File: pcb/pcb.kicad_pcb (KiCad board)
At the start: 4 copper layers, 107 parts, among them J1 Conn_02x10_Odd_Even, J2 Conn_02x03_Counter_Clockwise, Q1 BSS138, Q10 BSS138, Q11 BSS138, Q12 BSS138, Q2 BSS138, Q3 BSS138, Q4 BSS138, Q5 BSS138, Q6 BSS138, Q7 BSS138, Q8 BSS138, Q9 BSS138, SW1 SW_PUSHBUTTON, SW2 SW_PUSHBUTTON, SW3 SW_PUSHBUTTON, SW4 SW_PUSHBUTTON, U1 EFM32GG980, U2 ARDUINO_PYNQ_SHIELD, U3 IMU, U4 lidar, U5 ULTRASONIC-GPIO, U6 ULTRASONIC-GPIO, U7 ULTRASONIC-GPIO, Y1 Crystal_GND23

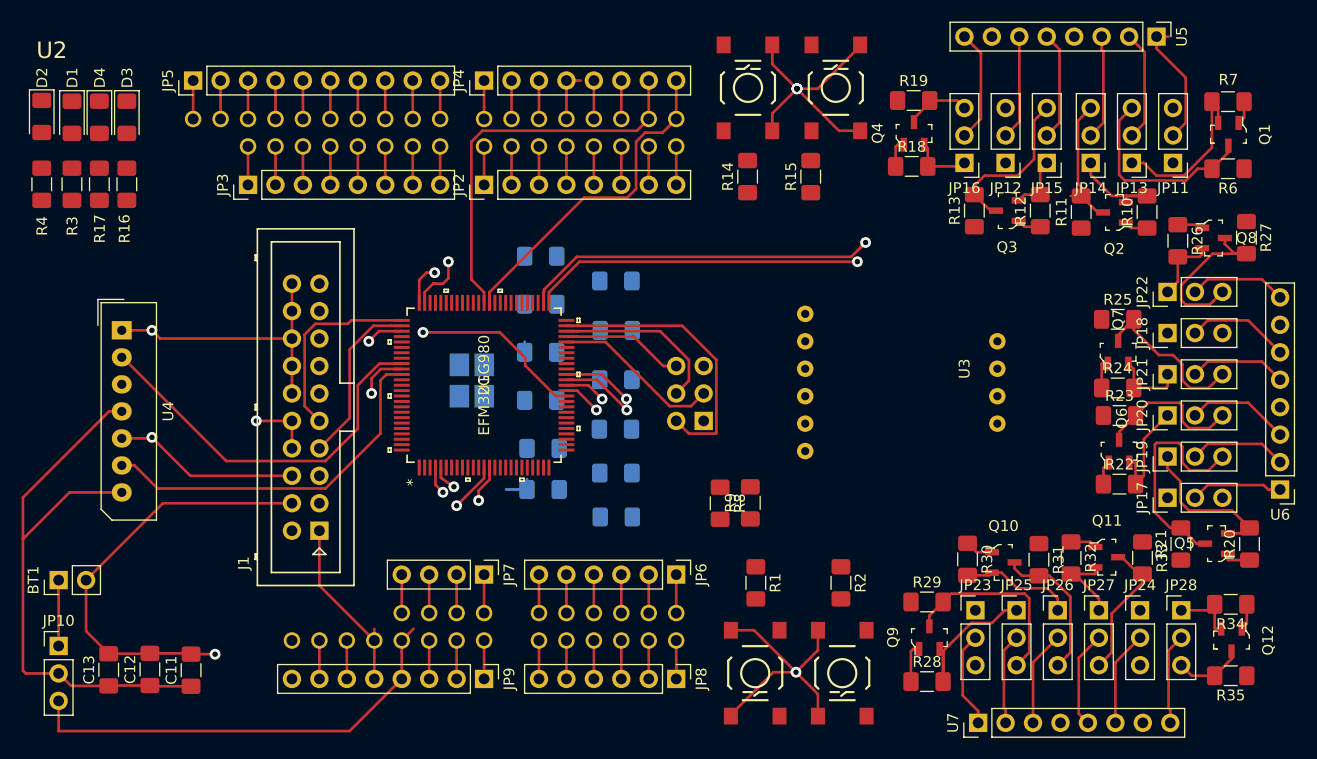
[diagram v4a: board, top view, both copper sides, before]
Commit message: Connect some more wires
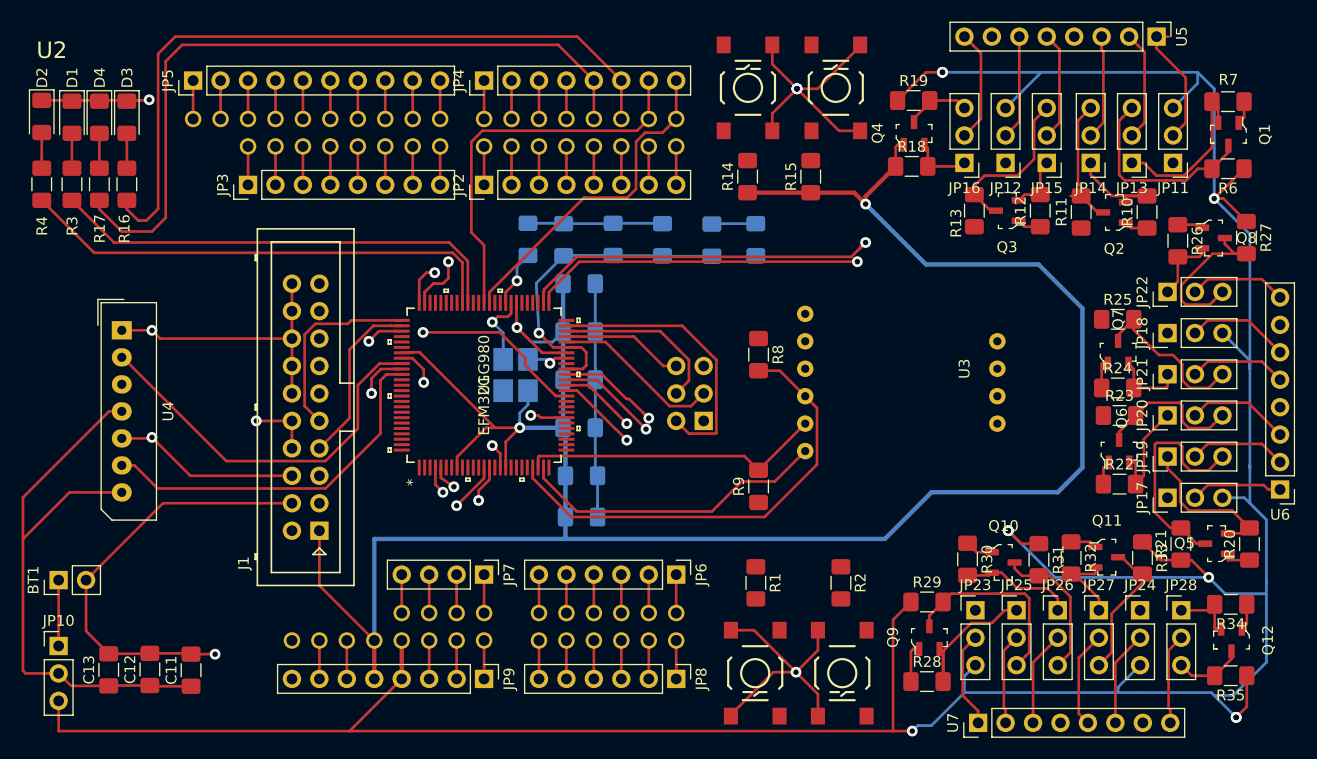
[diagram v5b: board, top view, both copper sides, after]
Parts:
- moved C10 27.0 mm to (105.7, 64.5), turned to 270 degrees
- moved L1 25.2 mm to (126.7, 64.5), turned to 90 degrees
- moved R5 19.6 mm to (122.7, 64.6), turned to 270 degrees
- moved R8 14.2 mm to (127.0, 75.1)
- moved C7 13.7 mm to (118.1, 64.5), turned to 90 degrees
- moved C5 8.42 mm to (113.5, 64.5), turned to 90 degrees
- moved C2 6.15 mm to (109.0, 64.5), turned to 90 degrees
- moved C3 4.37 mm to (110.4, 73.0)
- moved C6 4.37 mm to (110.4, 81.9)
- moved C8 4.37 mm to (110.6, 86.4)
- moved C9 4.37 mm to (110.6, 90.2)
- moved C1 4.37 mm to (110.4, 68.6)
- moved C4 4.37 mm to (110.4, 77.5)
- moved Y1 4.08 mm to (104.5, 77.0)
- moved R9 1.70 mm to (127.0, 87.3)
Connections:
- R1 pad 2: /EFM_DEBUG/SW_1 -> /PC1
- R2 pad 2: /EFM_DEBUG/SW_2 -> /PC0
- SW1 pad 1: /EFM_DEBUG/SW_1 -> /PC1
- SW2 pad 1: /EFM_DEBUG/SW_2 -> /PC0
- U1 pad 1: /EFM_DEBUG/LED_1 -> Net-(U1-Pad1)
- U1 pad 18: Net-(U1-Pad18) -> /PC0
- U1 pad 19: Net-(U1-Pad19) -> /PC1
- U1 pad 2: /EFM_DEBUG/LED_2 -> Net-(U1-Pad2)
- U1 pad 66: Net-(U1-Pad66) -> /EFM_DEBUG/LED_1
- U1 pad 67: Net-(U1-Pad67) -> /EFM_DEBUG/LED_2
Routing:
- net VCC: track 41.6 -> 301.4 mm, vias 0 -> 9
- net +3V3: track 51.4 -> 247.8 mm, vias 0 -> 3
- net GND: track 167.4 -> 232.9 mm, vias 8 -> 13
- net /PYNQ-DEBUG/LED_2: track 3.56 -> 68.0 mm
- net /PYNQ-DEBUG/LED_1: track 3.56 -> 67.7 mm
- net /EFM_DEBUG/LED_2: track 0.00 -> 45.0 mm
- net /IMU/SDA: track 0.00 -> 42.9 mm
- net /EFM_DEBUG/LED_1: track 0.00 -> 42.8 mm
- net /AVDD_DEC: track 0.15 -> 33.0 mm, vias 0 -> 1
- net /IMU/RST: track 0.00 -> 28.8 mm
- net /IMU/SCL: track 0.00 -> 28.1 mm
- net /PB9: track 68.8 -> 74.8 mm
- net /DEC: track 0.00 -> 5.25 mm, vias 0 -> 1
- net Net-(L1-Pad2): track 0.00 -> 4.08 mm
- net /CLOCK/HFXTAL_N: track 0.00 -> 3.90 mm, vias 0 -> 1
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
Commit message: Think it is somewhat finished
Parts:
- removed JP11, JP12, JP13, JP14, JP15, JP16, JP17, JP18, JP19, JP20, JP21, JP22, JP23, JP24, JP25, JP26, JP27, JP28: Jumper_NC_Dual, Connector_PinHeader_2.54mm:PinHeader_1x03_P2.54mm_Vertical
- added JP1: M08, Connector_PinHeader_2.54mm:PinHeader_1x08_P2.54mm_Vertical, F.Cu at (101.6, 59.2)
- added SW10: SW_2xSPDT, localization-footprints:CAS-D20TB, F.Cu at (160.5, 101.6)
- added SW11: SW_2xSPDT, localization-footprints:CAS-D20TB, F.Cu at (169.4, 101.6)
- added SW12: SW_PUSHBUTTON, myfootprint:SW_PUSHBUTTON_SMD, F.Cu at (129.8, 52.0)
- added SW13: SW_PUSHBUTTON, myfootprint:SW_PUSHBUTTON_SMD, F.Cu at (138.4, 52.0)
- added SW5: SW_2xSPDT, localization-footprints:CAS-D20TB, F.Cu at (167.4, 88.4)
- added SW6: SW_2xSPDT, localization-footprints:CAS-D20TB, F.Cu at (150.9, 52.8)
- added SW7: SW_2xSPDT, localization-footprints:CAS-D20TB, F.Cu at (167.4, 79.2)
- added SW8: SW_2xSPDT, localization-footprints:CAS-D20TB, F.Cu at (167.4, 70.1)
- added SW9: SW_2xSPDT, localization-footprints:CAS-D20TB, F.Cu at (151.6, 101.6)
- C11, C12, C13, Q1, Q10, Q11, Q12, Q2, Q3, Q4, Q5, Q6, Q7, Q8, Q9, R10, R11, R12, R13, R18, R19, R20, R21, R22, R23, R24, R25, R26, R27, R28, R29, R30, R31: moved to B.Cu
- JP4: value M08 -> M10; footprint Connector_PinHeader_2.54mm:PinHeader_1x08_P2.54mm_Vertical -> Connector_PinHeader_2.54mm:PinHeader_1x10_P2.54mm_Vertical
- JP5: value M10 -> M06; footprint Connector_PinHeader_2.54mm:PinHeader_1x10_P2.54mm_Vertical -> Connector_PinHeader_2.54mm:PinHeader_1x06_P2.54mm_Vertical
- JP6: value M06 -> M04; footprint Connector_PinHeader_2.54mm:PinHeader_1x06_P2.54mm_Vertical -> Connector_PinHeader_2.54mm:PinHeader_1x04_P2.54mm_Vertical
- JP7: value M04 -> M06; footprint Connector_PinHeader_2.54mm:PinHeader_1x04_P2.54mm_Vertical -> Connector_PinHeader_2.54mm:PinHeader_1x06_P2.54mm_Vertical
- JP8: value M06 -> M08; footprint Connector_PinHeader_2.54mm:PinHeader_1x06_P2.54mm_Vertical -> Connector_PinHeader_2.54mm:PinHeader_1x08_P2.54mm_Vertical
- JP9: value M08 -> Jumper_NC_Dual; footprint Connector_PinHeader_2.54mm:PinHeader_1x08_P2.54mm_Vertical -> Connector_PinHeader_2.54mm:PinHeader_1x03_P2.54mm_Vertical
- R14, R15, R16, R17: value R -> 10k; moved to B.Cu
- R32, R33, R34, R35: value 10k -> R
- R6: value 10k -> 2.2k; moved to B.Cu
- R7: value 10k -> 4.7k; moved to B.Cu
- R8: value 2.2k -> 10k; moved to B.Cu
- R9: value 4.7k -> 10k; moved to B.Cu
- SW3, SW4: value SW_PUSHBUTTON -> SW_2xSPDT; footprint myfootprint:SW_PUSHBUTTON_SMD -> localization-footprints:CAS-D20TB
- moved R35 115.7 mm to (65.5, 56.6), turned to 90 degrees
- moved R34 110.7 mm to (68.1, 56.6), turned to 90 degrees
- moved R17 93.3 mm to (159.0, 51.8), turned to 270 degrees
- moved R16 87.7 mm to (156.2, 56.4), turned to 180 degrees
- moved SW2 79.3 mm to (63.8, 69.3), turned to 0 degrees
- moved R2 71.7 mm to (70.6, 64.0)
- moved SW1 68.5 mm to (63.8, 77.5), turned to 0 degrees
- moved JP5 64.1 mm to (119.4, 95.8), turned to 270 degrees
- moved R1 62.6 mm to (73.2, 64.0)
- moved R9 57.7 mm to (172.5, 51.8), turned to 270 degrees
- moved R8 46.4 mm to (169.4, 56.4), turned to 180 degrees
- moved R15 45.5 mm to (168.9, 85.1), turned to 180 degrees
- moved R14 45.0 mm to (164.3, 82.3)
- moved R32 43.8 mm to (127.8, 60.5), turned to 90 degrees
- moved R21 43.1 mm to (152.4, 51.8), turned to 270 degrees
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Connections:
- JP10 pad 1: Net-(BT1-Pad1) -> Net-(C11-Pad1)
- JP10 pad 2: Net-(C11-Pad1) -> Net-(JP10-Pad2)
- JP3 pad 3: Net-(JP3-Pad3) -> /PYNQ-DEBUG/LED_2
- JP3 pad 4: Net-(JP3-Pad4) -> /PYNQ-DEBUG/LED_1
- JP3 pad 5: Net-(JP3-Pad5) -> /PYNQ-DEBUG/SW_2
- JP3 pad 6: Net-(JP3-Pad6) -> /PYNQ-DEBUG/SW_1
- JP3 pad 7: Net-(JP3-Pad7) -> /PYNQ_TX
- JP3 pad 8: Net-(JP3-Pad8) -> /PYNQ_RX
- JP4 pad 1: Net-(JP4-Pad1) -> /PYNQ_SCL
- JP4 pad 2: Net-(JP4-Pad2) -> /PYNQ_SDA
- JP4 pad 3: /PYNQ-DEBUG/SW_2 -> Net-(JP4-Pad3)
- JP4 pad 4: /PYNQ-DEBUG/SW_1 -> Net-(JP4-Pad4)
- JP4 pad 5: /PYNQ-DEBUG/LED_2 -> Net-(JP4-Pad5)
- JP4 pad 6: /PYNQ-DEBUG/LED_1 -> Net-(JP4-Pad6)
- JP4 pad 7: /PYNQ_TX -> Net-(JP4-Pad7)
- JP4 pad 8: /PYNQ_RX -> Net-(JP4-Pad8)
- JP5 pad 1: /PYNQ_SCL -> Net-(JP5-Pad1)
- JP5 pad 2: /PYNQ_SDA -> Net-(JP5-Pad2)
- JP8 pad 2: Net-(JP8-Pad2) -> GND
- JP8 pad 3: Net-(JP8-Pad3) -> GND
- JP8 pad 4: Net-(JP8-Pad4) -> VCC
- JP8 pad 5: Net-(JP8-Pad5) -> +3V3
- JP9 pad 1: Net-(JP9-Pad1) -> Net-(BT1-Pad1)
- JP9 pad 2: GND -> Net-(C11-Pad1)
- JP9 pad 3: GND -> VCC
- Q1 pad 2: /PD5 -> /PD6_A1
- Q1 pad 3: Net-(JP13-Pad3) -> Net-(Q1-Pad3)
- Q10 pad 2: /PB5 -> /PC1_B2
- Q10 pad 3: Net-(JP26-Pad3) -> Net-(Q10-Pad3)
- Q11 pad 2: /PA4 -> /PC3_BRX
- Q11 pad 3: Net-(JP27-Pad3) -> Net-(Q11-Pad3)
- Q12 pad 2: /PA3 -> /PC2_BTX
- Q12 pad 3: Net-(JP28-Pad3) -> Net-(Q12-Pad3)
- Q2 pad 2: /PD6 -> /PA7_C1
- Q3 pad 2: /PF11 -> /PD7_A2
- Q3 pad 3: Net-(JP15-Pad3) -> Net-(Q3-Pad3)
- Q4 pad 2: /PF10 -> /PA8_C2
- Q4 pad 3: Net-(JP16-Pad3) -> Net-(Q4-Pad3)
- Q5 pad 2: /PB11 -> /PF11_ARX
- Q5 pad 3: Net-(JP19-Pad3) -> Net-(Q5-Pad3)
- Q6 pad 2: /PB12 -> /PB8_CRX
- Q6 pad 3: Net-(JP20-Pad3) -> Net-(Q6-Pad3)
- Q7 pad 2: /PB10 -> /PF10_ATX
- Q7 pad 3: Net-(JP21-Pad3) -> Net-(Q7-Pad3)
- Q8 pad 2: /PB9 -> /PB7_CTX
- Q8 pad 3: Net-(JP22-Pad3) -> Net-(Q8-Pad3)
- Q9 pad 2: /PB4 -> /PC0_B1
- Q9 pad 3: Net-(JP25-Pad3) -> Net-(Q9-Pad3)
- R1 pad 2: /PC1 -> /EFM_DEBUG/SW_1
- R10 pad 2: /PD6 -> /PA7_C1
- R12 pad 2: /PF11 -> /PD7_A2
- R13 pad 2: Net-(JP15-Pad3) -> Net-(Q3-Pad3)
- R14 pad 2: /PYNQ-DEBUG/SW_1 -> /PA8_C2
- R15 pad 1: +3V3 -> VCC
- R15 pad 2: /PYNQ-DEBUG/SW_2 -> Net-(Q4-Pad3)
- R16 pad 1: /PYNQ-DEBUG/LED_1 -> +3V3
- R16 pad 2: Net-(D3-Pad2) -> /PF11_ARX
- R17 pad 1: /PYNQ-DEBUG/LED_2 -> VCC
- R17 pad 2: Net-(D4-Pad2) -> Net-(Q5-Pad3)
- R18 pad 2: /PF10 -> /PB8_CRX
- R19 pad 2: Net-(JP16-Pad3) -> Net-(Q6-Pad3)
- R2 pad 2: /PC0 -> /EFM_DEBUG/SW_2
- R20 pad 2: /PB11 -> /PF10_ATX
- R21 pad 2: Net-(JP19-Pad3) -> Net-(Q7-Pad3)
- R22 pad 2: /PB12 -> /PB7_CTX
- R23 pad 2: Net-(JP20-Pad3) -> Net-(Q8-Pad3)
- R24 pad 2: /PB10 -> /PC0_B1
- R25 pad 2: Net-(JP21-Pad3) -> Net-(Q9-Pad3)
- R26 pad 2: /PB9 -> /PC1_B2
- R27 pad 2: Net-(JP22-Pad3) -> Net-(Q10-Pad3)
- R28 pad 2: /PB4 -> /PC3_BRX
- R29 pad 2: Net-(JP25-Pad3) -> Net-(Q11-Pad3)
- R30 pad 2: /PB5 -> /PC2_BTX
- R31 pad 2: Net-(JP26-Pad3) -> Net-(Q12-Pad3)
- R32 pad 2: /PA4 -> /PYNQ-DEBUG/SW_1
- R33 pad 1: VCC -> +3V3
- R33 pad 2: Net-(JP27-Pad3) -> /PYNQ-DEBUG/SW_2
- R34 pad 1: +3V3 -> /PYNQ-DEBUG/LED_1
- R34 pad 2: /PA3 -> Net-(D3-Pad2)
- R35 pad 1: VCC -> /PYNQ-DEBUG/LED_2
- R35 pad 2: Net-(JP28-Pad3) -> Net-(D4-Pad2)
- R6 pad 1: VCC -> +3V3
- R6 pad 2: Net-(JP13-Pad3) -> /PB11_IMU_SDA
- R7 pad 2: /PD5 -> /PB12_IMU_SCL
- R8 pad 2: /IMU/SDA -> /PD6_A1
- R9 pad 1: +3V3 -> VCC
- R9 pad 2: /IMU/SCL -> Net-(Q1-Pad3)
- SW1 pad 1: /PC1 -> /EFM_DEBUG/SW_1
- SW2 pad 1: /PC0 -> /EFM_DEBUG/SW_2
- SW3 pad 1: /PYNQ-DEBUG/SW_1 -> VCC
- SW3 pad 2: GND -> Net-(SW3-Pad2)
- SW4 pad 1: /PYNQ-DEBUG/SW_2 -> Net-(Q3-Pad3)
- SW4 pad 2: GND -> Net-(SW4-Pad2)
- U1 pad 13: /PB4 -> Net-(U1-Pad13)
- U1 pad 14: /PB5 -> Net-(U1-Pad14)
- U1 pad 18: /PC0 -> /PC0_B1
- U1 pad 19: /PC1 -> /PC1_B2
- U1 pad 20: Net-(U1-Pad20) -> /PC2_BTX
- U1 pad 21: Net-(U1-Pad21) -> /PC3_BRX
- U1 pad 22: /IMU/SDA -> Net-(U1-Pad22)
- U1 pad 23: /IMU/SCL -> Net-(U1-Pad23)
- U1 pad 24: /IMU/RST -> /PB7_CTX
- U1 pad 25: Net-(U1-Pad25) -> /PB8_CRX
- U1 pad 26: Net-(U1-Pad26) -> /PA7_C1
- U1 pad 27: Net-(U1-Pad27) -> /PA8_C2
- U1 pad 28: Net-(U1-Pad28) -> /PA9_IMU_INT
- U1 pad 37: /PB9 -> Net-(U1-Pad37)
- U1 pad 38: /PB10 -> /PB10_IMU_RST
- U1 pad 39: /PB11 -> /PB11_IMU_SDA
- U1 pad 4: /PA3 -> Net-(U1-Pad4)
- U1 pad 40: /PB12 -> /PB12_IMU_SCL
- U1 pad 5: /PA4 -> Net-(U1-Pad5)
- U1 pad 51: /PD5 -> Net-(U1-Pad51)
- U1 pad 52: /PD6 -> /PD6_A1
- U1 pad 53: Net-(U1-Pad53) -> /PD7_A2
- U1 pad 66: /EFM_DEBUG/LED_1 -> Net-(U1-Pad66)
- U1 pad 67: /EFM_DEBUG/LED_2 -> Net-(U1-Pad67)
- U1 pad 68: Net-(U1-Pad68) -> /EFM_DEBUG/LED_1
- U1 pad 69: Net-(U1-Pad69) -> /EFM_DEBUG/LED_2
- U1 pad 70: Net-(U1-Pad70) -> /EFM_DEBUG/SW_2
- U1 pad 71: Net-(U1-Pad71) -> /EFM_DEBUG/SW_1
- U1 pad 74: /PF10 -> /PF10_ATX
- U1 pad 75: /PF11 -> /PF11_ARX
- U2 pad 10: Net-(JP5-Pad8) -> Net-(JP4-Pad8)
- U2 pad 11: Net-(JP5-Pad7) -> Net-(JP4-Pad7)
- U2 pad 12: Net-(JP5-Pad6) -> Net-(JP4-Pad6)
- U2 pad 13: Net-(JP5-Pad5) -> Net-(JP4-Pad5)
- U2 pad 2: /PYNQ-DEBUG/LED_1 -> /PYNQ-DEBUG/SW_1
- U2 pad 26: Net-(JP2-Pad8) -> Net-(JP1-Pad8)
- U2 pad 27: Net-(JP2-Pad7) -> Net-(JP1-Pad7)
- U2 pad 28: Net-(JP2-Pad6) -> Net-(JP1-Pad6)
- U2 pad 29: Net-(JP2-Pad5) -> Net-(JP1-Pad5)
- U2 pad 3: /PYNQ-DEBUG/LED_2 -> /PYNQ-DEBUG/SW_2
- U2 pad 30: Net-(JP2-Pad4) -> Net-(JP1-Pad4)
- U2 pad 31: Net-(JP2-Pad3) -> Net-(JP1-Pad3)
- U2 pad 32: Net-(JP2-Pad2) -> Net-(JP1-Pad2)
- U2 pad 33: Net-(JP2-Pad1) -> Net-(JP1-Pad1)
- U2 pad 34: Net-(JP3-Pad8) -> Net-(JP2-Pad8)
- U2 pad 35: Net-(JP3-Pad7) -> Net-(JP2-Pad7)
- U2 pad 36: Net-(JP3-Pad6) -> Net-(JP2-Pad6)
- U2 pad 37: Net-(JP3-Pad5) -> Net-(JP2-Pad5)
- U2 pad 38: Net-(JP3-Pad4) -> Net-(JP2-Pad4)
- U2 pad 39: Net-(JP3-Pad3) -> Net-(JP2-Pad3)
- U2 pad 4: /PYNQ-DEBUG/SW_1 -> /PYNQ-DEBUG/LED_1
- U2 pad 40: Net-(JP3-Pad2) -> Net-(JP2-Pad2)
- U2 pad 41: Net-(JP3-Pad1) -> Net-(JP2-Pad1)
- U2 pad 5: /PYNQ-DEBUG/SW_2 -> /PYNQ-DEBUG/LED_2
- U2 pad 6: Net-(JP4-Pad2) -> Net-(JP3-Pad2)
- U2 pad 7: Net-(JP4-Pad1) -> Net-(JP3-Pad1)
- U2 pad 8: Net-(JP5-Pad10) -> Net-(JP4-Pad10)
- U2 pad 9: Net-(JP5-Pad9) -> Net-(JP4-Pad9)
- U2 pad A0: Net-(JP8-Pad6) -> Net-(JP7-Pad6)
- U2 pad A1: Net-(JP8-Pad5) -> Net-(JP7-Pad5)
- U2 pad A10: Net-(JP6-Pad2) -> Net-(JP5-Pad2)
- U2 pad A11: Net-(JP6-Pad1) -> Net-(JP5-Pad1)
- U2 pad A2: Net-(JP8-Pad4) -> Net-(JP7-Pad4)
- U2 pad A3: Net-(JP8-Pad3) -> Net-(JP7-Pad3)
- U2 pad A4: Net-(JP8-Pad2) -> Net-(JP7-Pad2)
- U2 pad A5: Net-(JP8-Pad1) -> Net-(JP7-Pad1)
- U2 pad A6: Net-(JP6-Pad6) -> Net-(JP5-Pad6)
- U2 pad A7: Net-(JP6-Pad5) -> Net-(JP5-Pad5)
- U2 pad A8: Net-(JP6-Pad4) -> Net-(JP5-Pad4)
- U2 pad A9: Net-(JP6-Pad3) -> Net-(JP5-Pad3)
- U2 pad A_R: Net-(JP5-Pad3) -> Net-(JP4-Pad3)
- U2 pad G: Net-(JP5-Pad4) -> Net-(JP4-Pad4)
- U2 pad IO_R: Net-(JP9-Pad7) -> Net-(JP8-Pad7)
- U2 pad RST: Net-(JP9-Pad6) -> Net-(JP8-Pad6)
- U2 pad VIN: Net-(JP9-Pad1) -> Net-(JP8-Pad1)
- U2 pad V_N: Net-(JP7-Pad3) -> Net-(JP6-Pad3)
- U2 pad V_P: Net-(JP7-Pad4) -> Net-(JP6-Pad4)
- U2 pad XGND: Net-(JP7-Pad2) -> Net-(JP6-Pad2)
- U2 pad XV_R: Net-(JP7-Pad1) -> Net-(JP6-Pad1)
- U3 pad 1: /IMU/RST -> /PB10_IMU_RST
- U3 pad 2: /IMU/SCL -> /PB12_IMU_SCL
- U3 pad 3: /IMU/SDA -> /PB11_IMU_SDA
- U3 pad 9: /IMU/INT -> /PA9_IMU_INT
- U4 pad 4: Net-(C11-Pad1) -> Net-(JP10-Pad2)
- U5 pad 1: Net-(JP11-Pad2) -> Net-(SW3-Pad2)
- U5 pad 2: Net-(JP13-Pad2) -> Net-(SW3-Pad5)
- U5 pad 3: Net-(JP14-Pad2) -> Net-(SW4-Pad2)
- U5 pad 5: Net-(JP15-Pad2) -> Net-(SW4-Pad5)
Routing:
- net +3V3: track 247.8 -> 435.4 mm, vias 3 -> 12
- net /PA3: track 83.1 -> 0.00 mm, vias 1 -> 0
- net /PA4: track 78.2 -> 0.00 mm, vias 1 -> 0
- net /PC2_BTX: track 0.00 -> 78.0 mm, vias 0 -> 2
- net /PB7_CTX: track 0.00 -> 77.2 mm, vias 0 -> 1
- net /PD6_A1: track 0.00 -> 77.1 mm, vias 0 -> 1
- net /PD5: track 76.7 -> 0.00 mm, vias 1 -> 0
- net GND: track 232.9 -> 156.9 mm, vias 13 -> 10
- net /PB9: track 74.8 -> 0.00 mm, vias 1 -> 0
- net /PB4: track 74.7 -> 0.00 mm, vias 1 -> 0
- net /PF11_ARX: track 0.00 -> 74.3 mm, vias 0 -> 2
- net /PB11: track 73.2 -> 0.00 mm, vias 1 -> 0
- net /PB5: track 72.4 -> 0.00 mm, vias 1 -> 0
- net /PB8_CRX: track 0.00 -> 71.4 mm, vias 0 -> 1
- net /PF11: track 70.1 -> 0.00 mm, vias 1 -> 0
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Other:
- board outline added: 122.9 x 69.6 mm
- board text added: "SLAMdunk"
- board text added: "Thomas Aven Aslak Mkadmi Tord Standnes Jan Olav Moltu Daniel Romanich Ole Alexander Hole Sigve S. Nordgaard Hallvard Stemshaug Lasse Agentoft Eggen Odd Kristian Kvarmestøl"

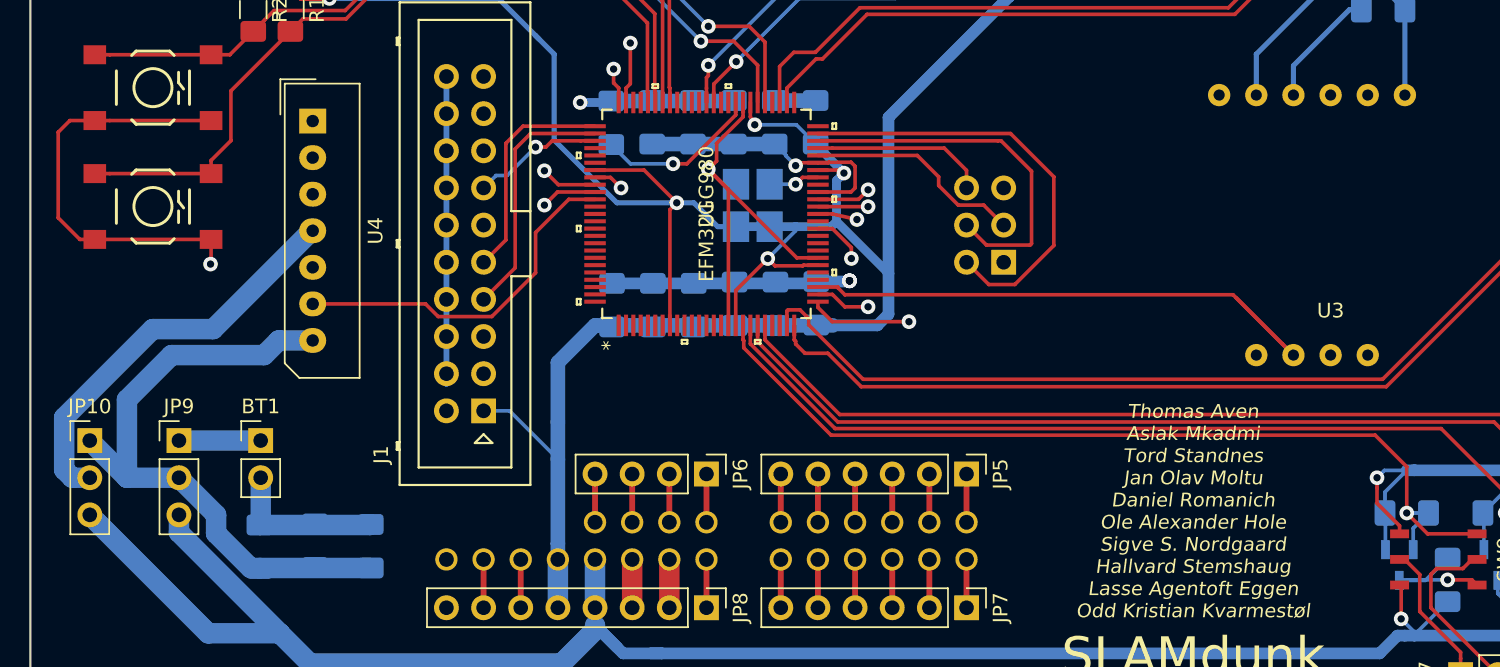
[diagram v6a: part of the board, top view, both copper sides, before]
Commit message: Fix pin silk and size of IMU
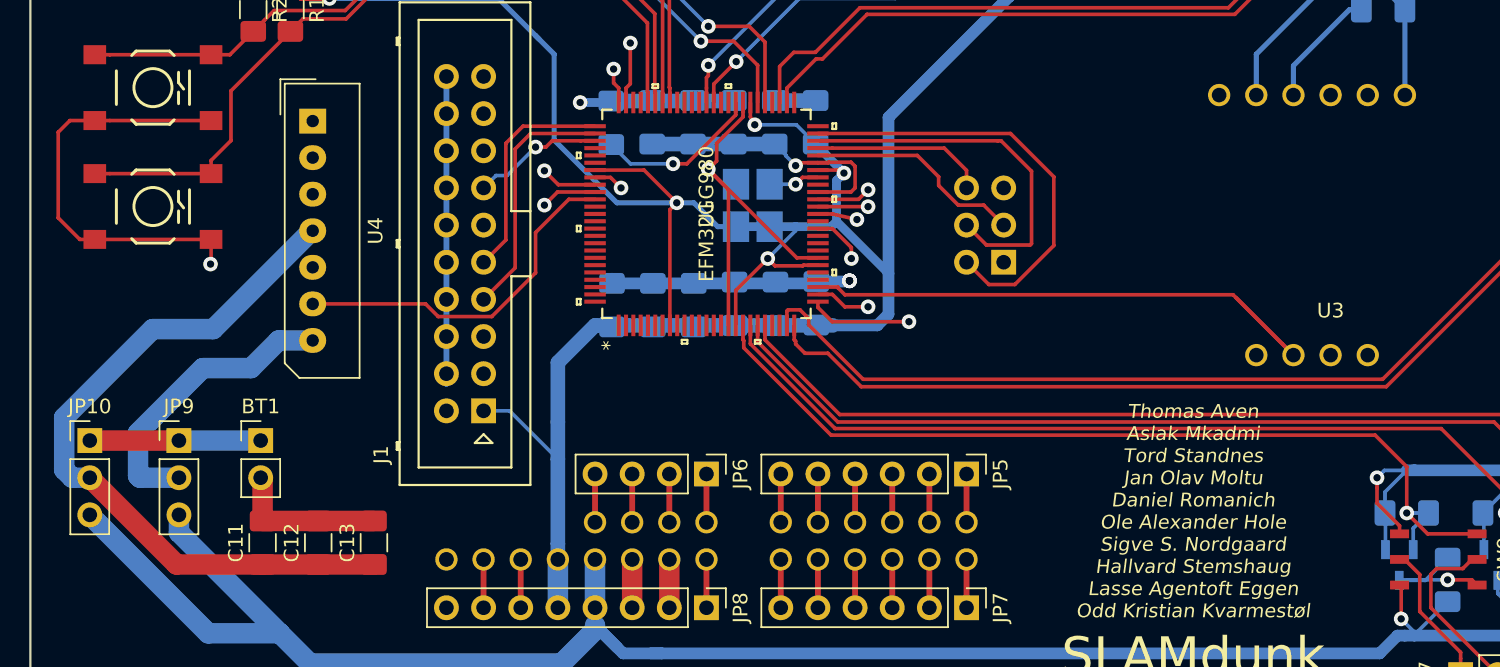
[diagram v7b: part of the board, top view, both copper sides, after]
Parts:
- C11, C12, C13: moved to F.Cu
- U3: footprint Adafruit BNO055:BNO055 -> Adafruit-BNO055-Breakout-PCB-master:BNO055
- moved C11 0.35 mm to (71.2, 100.5)
- moved C13 0.32 mm to (78.9, 100.5)
- moved C12 0.30 mm to (75.1, 100.5)
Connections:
- JP10 pad 1: Net-(C11-Pad1) -> Net-(BT1-Pad1)
- JP10 pad 2: Net-(JP10-Pad2) -> Net-(C11-Pad1)
- JP9 pad 2: Net-(C11-Pad1) -> Net-(JP9-Pad2)
- U4 pad 4: Net-(JP10-Pad2) -> Net-(C11-Pad1)
- U4 pad 7: Net-(C11-Pad1) -> Net-(JP9-Pad2)
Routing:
- net Net-(JP10-Pad2): track 27.8 -> 0.00 mm
- net Net-(JP9-Pad2): track 0.00 -> 20.3 mm
- net Net-(C11-Pad1): track 43.3 -> 49.7 mm
- net Net-(BT1-Pad1): track 5.59 -> 11.7 mm
- added copper zone on GND.Cu, net GND
- removed copper zone on GND, net GND

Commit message: Fix design rules
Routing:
- net /AVDD_DEC: track 18.9 -> 21.4 mm
- net /PB11_IMU_SDA: track 44.3 -> 45.5 mm
- net Net-(Q9-Pad3): track 9.41 -> 8.23 mm
- net /PYNQ_SCL: track 45.2 -> 45.9 mm
